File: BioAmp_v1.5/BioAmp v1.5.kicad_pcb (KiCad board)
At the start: 2 copper layers, 32 x 60 mm, 33 parts, among them J1 Conn_01x02_Male, J2 PJ-3062-CO, J4 Conn_01x03_Male, J5 Conn_01x02_Male, J6 Conn_01x02_Male, J7 Conn_01x02_Male, U1 TL074

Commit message: update v1.5.4
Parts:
- removed the REF** at (115.9, 103.9) (x2)
- added C8: CP, Capacitor_THT:CP_Radial_D5.0mm_P2.50mm, F.Cu at (153.4, 88.1)
- added REF**: OSHW-Logo2_9.8x8mm_SilkScreen, Symbol:OSHW-Logo2_9.8x8mm_SilkScreen, F.Cu at (150.3, 121.6)
- added REF**: OSHW-Logo2_9.8x8mm_SilkScreen, Symbol:OSHW-Logo2_9.8x8mm_SilkScreen, B.Cu at (150.3, 121.6)
- C2: value 100nf -> CP; footprint Capacitor_THT:C_Disc_D3.8mm_W2.6mm_P2.50mm -> Capacitor_THT:CP_Radial_D5.0mm_P2.50mm
- S1: footprint udlabs:TL2285EE -> udlabs:G64_DPDT
- moved R7 55.6 mm to (145.5, 118.0), turned to 90 degrees
- moved J1 49.6 mm to (151.5, 99.8)
- moved C1 47.9 mm to (142.6, 111.6), turned to 180 degrees
- moved S1 39.7 mm to (151.6, 111.0)
- moved J5 39.3 mm to (148.8, 104.5)
- moved J5 39.3 mm to (145.0, 104.4)
- moved J7 38.6 mm to (139.2, 119.5)
- moved J7 38.6 mm to (139.2, 115.8)
- moved D1 38.2 mm to (133.5, 116.2)
- moved G*** 38.2 mm to (130.9, 122.2)
- moved C2 38.1 mm to (147.0, 88.2), turned to 180 degrees
- moved C7 37.9 mm to (126.8, 118.5)
- moved C4 37.6 mm to (132.6, 108.2)
- moved R11 37.6 mm to (129.7, 104.9)
- moved C5 37.6 mm to (137.4, 108.2)
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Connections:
- C2 pad 1: ACout -> Aout
- C2 pad 2: Aout -> ACout
- J2 pad 2: ACout -> ACout_spkr
- J2 pad 3: ACout -> ACout_spkr
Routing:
- net ACout_spkr: track 0.00 -> 22.1 mm
- net GND: track 88.0 -> 70.9 mm
- net Aout: track 29.5 -> 46.2 mm
- net ACout: track 46.6 -> 32.2 mm
- net Net-(C3-Pad1): track 20.0 -> 34.1 mm
- net Net-(J1-Pad1): track 20.2 -> 31.1 mm
- net +9V: track 59.9 -> 68.6 mm
- net Vref: track 84.3 -> 77.4 mm
- net B-: track 17.8 -> 21.6 mm
- net Net-(D1-Pad1): track 13.4 -> 15.5 mm
- net Net-(C4-Pad1): track 37.5 -> 36.1 mm
- net B+: track 12.6 -> 13.9 mm
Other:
- board text added: "AUXOUT"
- board text added: "S"

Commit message: Update to v1.5.5
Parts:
- removed the REF** at (150.3, 121.6)
- added G***: LOGO, udlabs:OSHWA_IN000019_9.1x6.7, B.Cu at (150.5, 122.0)
- C1, C3: value 100nf -> 4.7nf
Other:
- board text added: "DEC 2020"
- board text added: "Rev 1.5.5"
- board text removed: "NOV 2020"

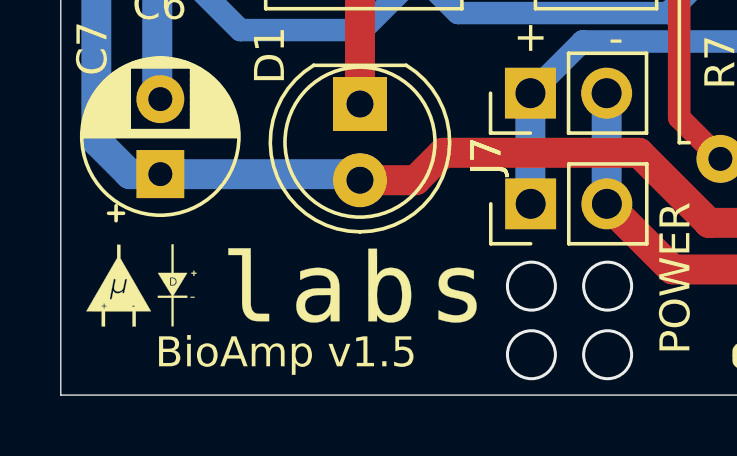
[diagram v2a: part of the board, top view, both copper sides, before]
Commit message: BioAmp v1.5.6 KiCAD PCB
This version includes minor cosmetic changes,
this will be the final revision of BioAmp v1.5!
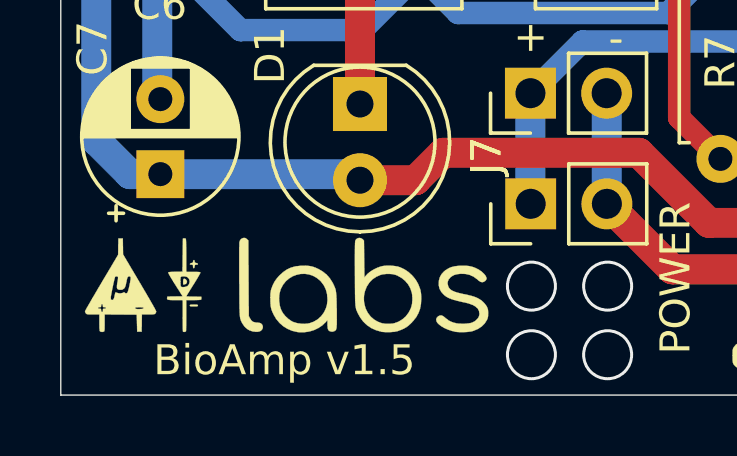
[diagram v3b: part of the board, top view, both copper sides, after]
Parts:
- removed the G*** at (130.9, 122.2)
- added G***: LOGO, udlabs:udlabsNew_13.4x3.2mm, F.Cu at (131.0, 122.2)
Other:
- board text added: "AUXOUT EARPHONES"
- board text added: "JULY 2021"
- board text added: "Rev 1.5.6"
- board text removed: "AUXOUT"
- board text removed: "DEC 2020"
- board text removed: "Rev 1.5.5"
